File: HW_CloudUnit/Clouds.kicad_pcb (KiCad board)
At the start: 2 copper layers, 0 parts

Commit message: (WIP) Layout of driver board
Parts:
- added C1: 4.7u, Capacitor_SMD:C_0603_1608Metric, B.Cu at (22.6, 23.2)
- added C2: 100n, Capacitor_SMD:C_0603_1608Metric, B.Cu at (24.1, 23.2)
- added C3: 100n, Capacitor_SMD:C_0603_1608Metric, B.Cu at (24.6, 32.2)
- added C4: 10n, Capacitor_SMD:C_0603_1608Metric, F.Cu at (32.6, 34.1)
- added C5: 470n, Capacitor_SMD:C_0603_1608Metric, F.Cu at (36.2, 42.2)
- added C6: 100n, Capacitor_SMD:C_0603_1608Metric, F.Cu at (26.2, 36.6)
- added C7: 10u, Capacitor_SMD:CP_Elec_5x3.9, F.Cu at (27.7, 31.9)
- added D1: White, LED_SMD:LED_0603_1608Metric, F.Cu at (36.1, 34.2)
- added D2: Green, LED_SMD:LED_0603_1608Metric, F.Cu at (37.6, 34.2)
- added D3: Yellow, LED_SMD:LED_0603_1608Metric, F.Cu at (39.1, 34.2)
- added G***: LOGO, LOGO, F.Cu at (46.6, 13.7)
- added G***: LOGO, LOGO, B.Cu at (31.4, 65.4)
- added G***: LOGO, LOGO, B.Cu at (23.7, 63.8)
- added G***: LOGO, LOGO, B.Cu at (28.2, 64.1)
- added J1: Conn_01x06, Connector_PinHeader_2.54mm:PinHeader_1x06_P2.54mm_Vertical, F.Cu at (20.0, 32.7)
- added J2: Conn_01x04, Connector_JST:JST_GH_SM04B-GHS-TB_1x04-1MP_P1.25mm_Horizontal, F.Cu at (21.1, 40.2)
- added J3: Conn_01x04, Connector_PinHeader_2.00mm:PinHeader_1x04_P2.00mm_Vertical, F.Cu at (38.8, 19.8)
- added J4: Conn_01x04, Clouds_footprints:TestPoints_1x04_P2.0, F.Cu at (29.2, 19.6)
- added JP1: SolderJumper_2_Open, Jumper:SolderJumper-2_P1.3mm_Open_RoundedPad1.0x1.5mm, F.Cu at (38.4, 42.2)
- added R1: 100k, Resistor_SMD:R_0603_1608Metric, B.Cu at (34.7, 19.7)
- added R2: 2.2k, Resistor_SMD:R_0603_1608Metric, B.Cu at (35.3, 30.0)
- added R3: 2.2k, Resistor_SMD:R_0603_1608Metric, B.Cu at (33.8, 30.0)
- added R4: TBD, Resistor_SMD:R_0603_1608Metric, F.Cu at (36.1, 37.2)
- added R5: TBD, Resistor_SMD:R_0603_1608Metric, F.Cu at (37.6, 37.2)
- added R6: TBD, Resistor_SMD:R_0603_1608Metric, F.Cu at (39.1, 37.2)
- added R7: TBD, Resistor_SMD:R_0603_1608Metric, B.Cu at (35.4, 21.8)
- added R8: TBD, Resistor_SMD:R_0603_1608Metric, B.Cu at (35.4, 23.8)
- added R9: TBD, Resistor_SMD:R_0603_1608Metric, B.Cu at (35.4, 25.8)
- added U1: STM32G030F6Px, Package_SO:TSSOP-20_4.4x6.5mm_P0.65mm, B.Cu at (28.7, 24.2)
- added U2: AS5600L-ASOM, Clouds_footprints:SOIC127P600X175-8N, B.Cu at (29.2, 32.7)
- added U3: DRV8313PWPR, Clouds_footprints:SOP65P640X120-29N, F.Cu at (31.2, 39.9)
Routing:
- net NFAULT: track 0.00 -> 8.37 mm
- net MOTOR_W: track 0.00 -> 6.11 mm
- net Net-(U3-CPH): track 0.00 -> 6.05 mm
- net V3P3O: track 0.00 -> 5.66 mm
- net MOTOR_U: track 0.00 -> 5.32 mm
- net MOTOR_V: track 0.00 -> 5.06 mm
- net Net-(U3-CPL): track 0.00 -> 4.23 mm
- net Net-(U3-VCP): track 0.00 -> 2.54 mm
- net GND: track 0.00 -> 0.82 mm, vias 0 -> 22
- added copper zone on B.Cu, net GND
- added copper zone on F.Cu, net GND
- added copper zone on F.Cu, net V3P3O
- added copper zone on F.Cu, net VM
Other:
- board outline added: 22 x 27 mm
- board text added: "*"
- board text added: "+"
- board text added: "23-Flurry"
- board text added: "3V3"
- board text added: "B"
- board text added: "BLDC Driver (Y-wired) Magnet Encoder"
- board text added: "BLDC on Clouds"
- board text added: "CM"
- board text added: "CSN"
- board text added: "G"
- board text added: "GND"
- board text added: "Input 8-60 V Output 1.75 A RMS"
- board text added: "JLCJLCJLCJLC"
- board text added: "R"
- board text added: "Rev. 1"
- board text added: "SCK"
- board text added: "SDA"
- board text added: "U"
- board text added: "V"
- board text added: "VM"
- board text added: "W"

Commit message: (WIP) Try routing
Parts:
- moved R4 3.40 mm to (36.1, 33.8)
- moved R5 3.40 mm to (37.6, 33.8)
- moved R6 3.40 mm to (39.1, 33.8)
- moved D1 3.40 mm to (36.1, 30.8)
- moved D2 3.40 mm to (37.6, 30.8)
- moved D3 3.40 mm to (39.1, 30.8)
- moved C1 1.70 mm to (22.6, 24.9), turned to 90 degrees
- moved C2 1.70 mm to (24.1, 24.9), turned to 90 degrees
- moved R2 1.30 mm to (35.2, 31.3)
- moved R3 1.30 mm to (33.7, 31.3)
- turned U1 to 0 degrees
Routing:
- net +3.3V: track 0.00 -> 79.6 mm, vias 0 -> 2
- net LED_ACT: track 0.00 -> 20.9 mm, vias 0 -> 1
- net SWCLK: track 0.00 -> 14.2 mm
- net NFAULT: track 8.37 -> 20.2 mm
- net UNIT_CSN: track 0.00 -> 11.6 mm
- net LED_B: track 0.00 -> 9.51 mm, vias 0 -> 2
- net SWDIO: track 0.00 -> 7.46 mm, vias 0 -> 1
- net UNIT_SDA: track 0.00 -> 6.37 mm
- net UNIT_SCK: track 0.00 -> 6.12 mm
- net LED_G: track 0.00 -> 5.00 mm
- net V3P3O: track 5.66 -> 10.5 mm
- net MAG_SCL: track 0.00 -> 3.80 mm
- net EN_U: track 0.00 -> 3.66 mm, vias 0 -> 1
- net LED_R: track 0.00 -> 3.23 mm
- net IN_U: track 0.00 -> 3.01 mm, vias 0 -> 1
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- added copper zone on B.Cu, net +3.3V

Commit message: Finish driver board design
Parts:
- moved G*** 21.7 mm to (28.9, 43.9)
- moved G*** 21.7 mm to (21.2, 42.3)
- moved G*** 21.7 mm to (25.7, 42.6)
- moved G*** 13.9 mm to (36.8, 23.6)
- moved D1 5.00 mm to (41.1, 30.8)
- moved D2 5.00 mm to (42.6, 30.8)
- moved D3 5.00 mm to (44.1, 30.8)
- moved J3 5.00 mm to (43.8, 19.8)
- moved R4 5.00 mm to (41.1, 33.8)
- moved R5 5.00 mm to (42.6, 33.8)
- moved R6 5.00 mm to (44.1, 33.8)
- moved R7 5.00 mm to (40.4, 21.8)
- moved R8 5.00 mm to (40.4, 23.8)
- moved R9 5.00 mm to (40.4, 25.8)
- moved J4 3.50 mm to (32.7, 19.7)
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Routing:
- net EN_U: track 3.66 -> 24.7 mm
- net EN_W: track 0.00 -> 20.0 mm, vias 0 -> 1
- net EN_V: track 2.38 -> 22.3 mm
- net IN_U: track 3.01 -> 21.1 mm
- net MAG_SCL: track 3.80 -> 20.5 mm
- net IN_V: track 1.76 -> 18.5 mm
- net IN_W: track 0.00 -> 15.6 mm, vias 0 -> 1
- net MAG_SDA: track 1.82 -> 17.2 mm
- net LED_B: track 9.51 -> 17.4 mm
- net LED_ACT: track 20.9 -> 28.8 mm
- net +3.3V: track 79.6 -> 72.7 mm
- net UNIT_SCK: track 6.12 -> 9.62 mm
- net UNIT_SDA: track 6.37 -> 9.87 mm
- net UNIT_CSN: track 11.6 -> 15.1 mm
- net SWCLK: track 14.2 -> 17.2 mm
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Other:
- board size 22 x 27 mm -> 27 x 27 mm
- board text added: "BLDC (Y-wired) + Mag. Enc."
- board text added: "Close for on-board 3V3 reg."
- board text added: "In 8-50 V Out 1.75 A RMS"
- board text added: "Rev. 2"
- board text removed: "BLDC Driver (Y-wired) Magnet Encoder"
- board text removed: "Input 8-60 V Output 1.75 A RMS"
- board text removed: "Rev. 1"

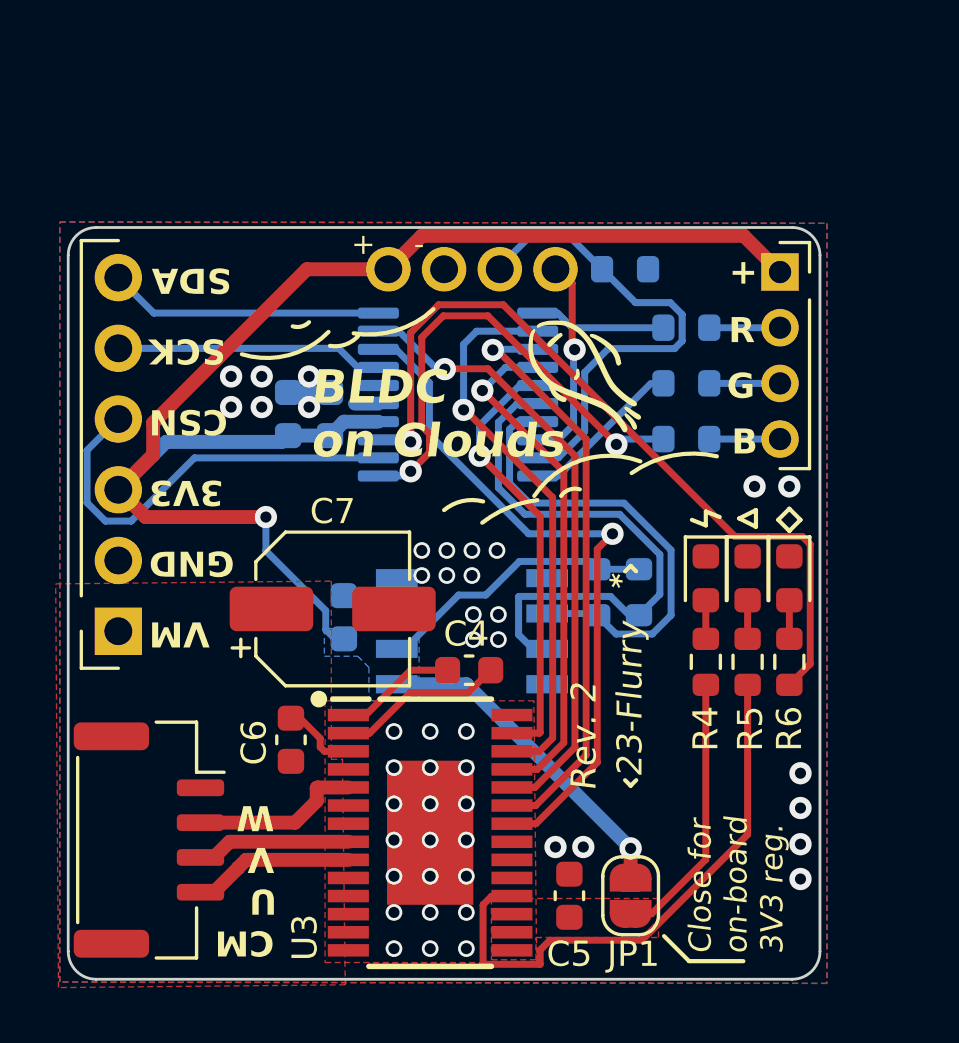
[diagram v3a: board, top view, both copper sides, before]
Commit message: Fix motor's wire order
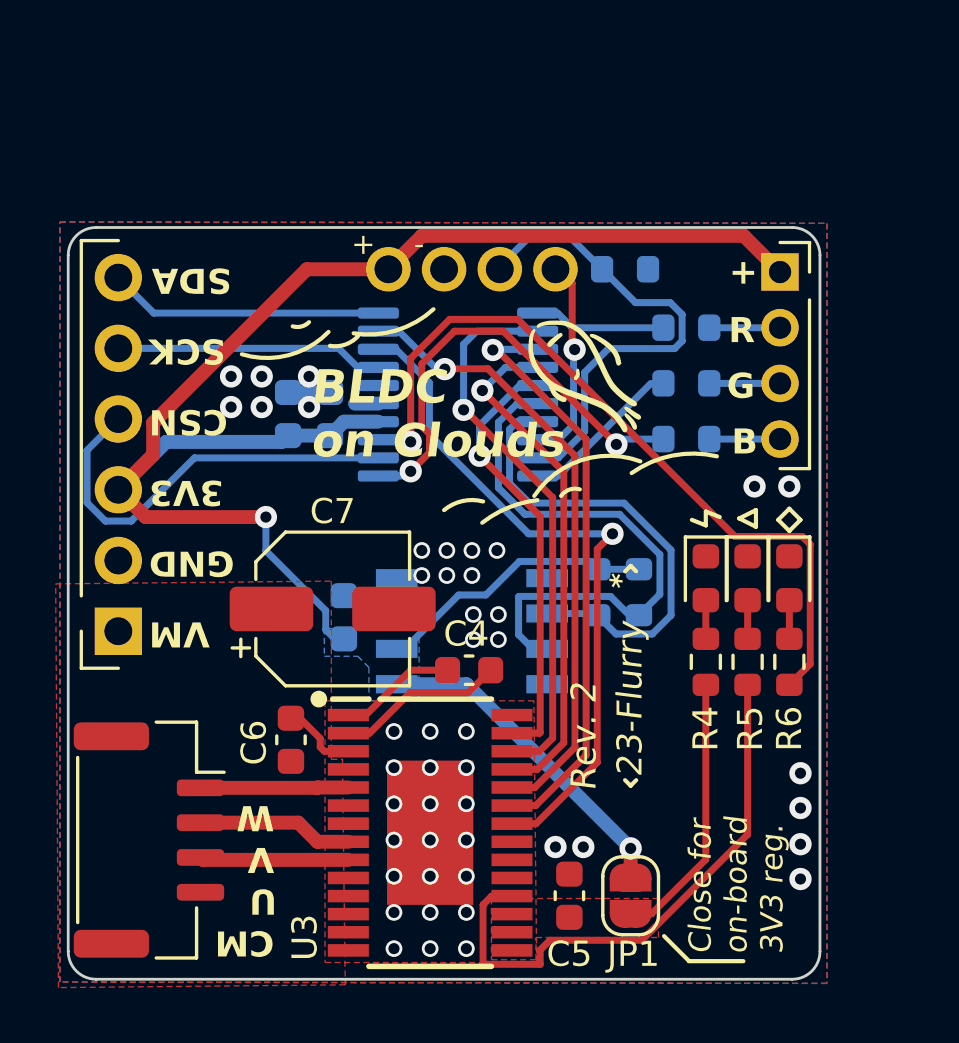
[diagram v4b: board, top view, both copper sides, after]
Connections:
- J2 pad 1: unconnected-(J2-Pin_1-Pad1) -> MOTOR_W
- J2 pad 2: MOTOR_W -> MOTOR_V
- J2 pad 3: MOTOR_V -> MOTOR_U
- J2 pad 4: MOTOR_U -> unconnected-(J2-Pin_4-Pad4)
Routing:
- net LED_B: track 17.4 -> 16.4 mm
- net LED_ACT: track 28.8 -> 27.8 mm
- net MOTOR_W: track 6.11 -> 5.32 mm
- net MOTOR_V: track 5.06 -> 5.60 mm
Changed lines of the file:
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@@
   (net 38 "Net-(J3-Pin_4)")
   (net 39 "V3P3O")
-  (net 40 "unconnected-(J2-Pin_1-Pad1)")
+  (net 40 "unconnected-(J2-Pin_4-Pad4)")
   (footprint "Connector_JST:JST_GH_SM04B-GHS-TB_1x04-1MP_P1.25mm_Horizontal" (layer "F.Cu")
     (at 21.1 40.2 -90)
@@
       (stroke (width 0.1) (type solid)) (layer "F.Fab"))
     (pad "1" smd roundrect (at -1.875 -1.85 270) (size 0.6 1.7) (layers "F.Cu" "F.Paste" "F.Mask") (roundrect_rratio 0.25)
-      (net 40 "unconnected-(J2-Pin_1-Pad1)") (pinfunction "Pin_1") (pintype "passive+no_connect"))
+      (net 15 "MOTOR_W") (pinfunction "Pin_1") (pintype "passive"))
     (pad "2" smd roundrect (at -0.625 -1.85 270) (size 0.6 1.7) (layers "F.Cu" "F.Paste" "F.Mask") (roundrect_rratio 0.25)
-      (net 15 "MOTOR_W") (pinfunction "Pin_2") (pintype "passive"))
+      (net 14 "MOTOR_V") (pinfunction "Pin_2") (pintype "passive"))
     (pad "3" smd roundrect (at 0.625 -1.85 270) (size 0.6 1.7) (layers "F.Cu" "F.Paste" "F.Mask") (roundrect_rratio 0.25)
-      (net 14 "MOTOR_V") (pinfunction "Pin_3") (pintype "passive"))
+      (net 13 "MOTOR_U") (pinfunction "Pin_3") (pintype "passive"))
     (pad "4" smd roundrect (at 1.875 -1.85 270) (size 0.6 1.7) (layers "F.Cu" "F.Paste" "F.Mask") (roundrect_rratio 0.25)
-      (net 13 "MOTOR_U") (pinfunction "Pin_4") (pintype "passive"))
+      (net 40 "unconnected-(J2-Pin_4-Pad4)") (pinfunction "Pin_4") (pintype "passive+no_connect"))
     (pad "MP" smd roundrect (at -3.725 1.35 270) (size 1 2.7) (layers "F.Cu" "F.Paste" "F.Mask") (roundrect_rratio 0.25))
     (pad "MP" smd roundrect (at 3.725 1.35 270) (size 1 2.7) (layers "F.Cu" "F.Paste" "F.Mask") (roundrect_rratio 0.25))
@@
   (segment (start 34.409314 23.875) (end 35.0625 23.875) (width 0.25) (layer "B.Cu") (net 12))
   (segment (start 32.9755 25.308814) (end 34.409314 23.875) (width 0.25) (layer "B.Cu") (net 12))
-  (segment (start 28.262 40.9125) (end 24.5875 40.9125) (width 0.5) (layer "F.Cu") (net 13))
-  (segment (start 24.5875 40.9125) (end 24.3 41.2) (width 0.5) (layer "F.Cu") (net 13))
-  (segment (start 24.3 41.2) (end 24.3 41.206974) (width 0.5) (layer "F.Cu") (net 13))
-  (segment (start 24.3 41.206974) (end 23.431974 42.075) (width 0.5) (layer "F.Cu") (net 13))
-  (segment (start 28.262 40.2625) (end 23.994474 40.2625) (width 0.5) (layer "F.Cu") (net 14))
-  (segment (start 23.994474 40.2625) (end 23.431974 40.825) (width 0.5) (layer "F.Cu") (net 14))
+  (segment (start 23.0375 40.9125) (end 28.262 40.9125) (width 0.5) (layer "F.Cu") (net 13))
+  (segment (start 22.95 40.825) (end 23.0375 40.9125) (width 0.5) (layer "F.Cu") (net 13))
+  (segment (start 26.462 39.575) (end 27.1495 40.2625) (width 0.5) (layer "F.Cu") (net 14))
+  (segment (start 27.1495 40.2625) (end 28.262 40.2625) (width 0.5) (layer "F.Cu") (net 14))
+  (segment (start 22.95 39.575) (end 26.462 39.575) (width 0.5) (layer "F.Cu") (net 14))
   (segment (start 28.262 38.3125) (end 27.1495 38.3125) (width 0.5) (layer "F.Cu") (net 15))
-  (segment (start 27.1495 38.3125) (end 27.1245 38.3375) (width 0.5) (layer "F.Cu") (net 15))
-  (segment (start 27.1245 38.3375) (end 27.1245 38.8) (width 0.5) (layer "F.Cu") (net 15))
-  (segment (start 27.1245 38.8) (end 26.3495 39.575) (width 0.5) (layer "F.Cu") (net 15))
-  (segment (start 26.3495 39.575) (end 22.95 39.575) (width 0.5) (layer "F.Cu") (net 15))
+  (segment (start 27.1495 38.3125) (end 27.137 38.325) (width 0.5) (layer "F.Cu") (net 15))
+  (segment (start 27.137 38.325) (end 22.95 38.325) (width 0.5) (layer "F.Cu") (net 15))
   (segment (start 42.6 34.625) (end 42.6 40.001468) (width 0.25) (layer "F.Cu") (net 16))
   (segment (start 35.5 43.8) (end 35.1505 44.1495) (width 0.25) (layer "F.Cu") (net 16))
@@
   (segment (start 39.124999 23.8) (end 35.799999 27.125) (width 0.25) (layer "B.Cu") (net 22))
   (segment (start 35.799999 27.125) (end 35.0625 27.125) (width 0.25) (layer "B.Cu") (net 22))
-  (segment (start 30.9 22.145405) (end 30.9 25.345405) (width 0.25) (layer "F.Cu") (net 24))
+  (segment (start 31.175 26.282819) (end 30.500978 26.956841) (width 0.25) (layer "F.Cu") (net 24))
   (segment (start 30.9 25.345405) (end 31.175 25.620405) (width 0.25) (layer "F.Cu") (net 24))
-  (segment (start 33.275 21.375) (end 31.670405 21.375) (width 0.25) (layer "F.Cu") (net 24))
-  (segment (start 37.8875 25.991388) (end 37.8875 25.9875) (width 0.25) (layer "F.Cu") (net 24))
   (segment (start 31.175 25.620405) (end 31.175 26.282819) (width 0.25) (layer "F.Cu") (net 24))
-  (segment (start 31.670405 21.375) (end 30.9 22.145405) (width 0.25) (layer "F.Cu") (net 24))
-  (segment (start 31.175 26.282819) (end 30.500978 26.956841) (width 0.25) (layer "F.Cu") (net 24))
-  (segment (start 37.8875 25.9875) (end 33.275 21.375) (width 0.25) (layer "F.Cu") (net 24))
+  (segment (start 37.8875 25.9875) (end 33.8245 21.9245) (width 0.25) (layer "F.Cu") (net 24))
+  (segment (start 32.0755 21.9245) (end 30.9 23.1) (width 0.25) (layer "F.Cu") (net 24))
+  (segment (start 37.8875 25.991388) (end 37.8875 25.9875) (width 0.25) (layer "F.Cu") (net 24))
+  (segment (start 30.9 23.1) (end 30.9 25.345405) (width 0.25) (layer "F.Cu") (net 24))
+  (segment (start 33.8245 21.9245) (end 32.0755 21.9245) (width 0.25) (layer "F.Cu") (net 24))
   (via (at 37.8875 25.991388) (size 0.8) (drill 0.4) (layers "F.Cu" "B.Cu") (net 24))
   (via (at 30.500978 26.956841) (size 0.8) (drill 0.4) (layers "F.Cu" "B.Cu") (net 24))
@@
   (segment (start 35.0625 25.175) (end 34.325001 25.175) (width 0.25) (layer "B.Cu") (net 28))
   (segment (start 34.05 27.383102) (end 34.766898 28.1) (width 0.25) (layer "B.Cu") (net 28))
-  (segment (start 30.5 21.979719) (end 31.50472 20.975) (width 0.25) (layer "F.Cu") (net 29))
-  (segment (start 30.5 25.9) (end 30.5 21.979719) (width 0.25) (layer "F.Cu") (net 29))
-  (segment (start 44.56683 29.3) (end 44.85 29.58317) (width 0.25) (layer "F.Cu") (net 29))
-  (segment (start 44.85 33.875) (end 44.1 34.625) (width 0.25) (layer "F.Cu") (net 29))
   (segment (start 44.85 29.58317) (end 44.85 33.875) (width 0.25) (layer "F.Cu") (net 29))
-  (segment (start 31.50472 20.975) (end 33.825 20.975) (width 0.25) (layer "F.Cu") (net 29))
-  (segment (start 33.825 20.975) (end 42.15 29.3) (width 0.25) (layer "F.Cu") (net 29))
   (segment (start 42.15 29.3) (end 44.56683 29.3) (width 0.25) (layer "F.Cu") (net 29))
+  (segment (start 44.56683 29.3) (end 44.85 29.58317) (width 0.25) (layer "F.Cu") (net 29))
+  (segment (start 31.9 21.5) (end 34.35 21.5) (width 0.25) (layer "F.Cu") (net 29))
+  (segment (start 30.5 22.9) (end 31.9 21.5) (width 0.25) (layer "F.Cu") (net 29))
+  (segment (start 30.5 25.9) (end 30.5 22.9) (width 0.25) (layer "F.Cu") (net 29))
+  (segment (start 44.85 33.875) (end 44.1 34.625) (width 0.25) (layer "F.Cu") (net 29))
+  (segment (start 34.35 21.5) (end 42.15 29.3) (width 0.25) (layer "F.Cu") (net 29))
   (via (at 30.5 25.9) (size 0.8) (drill 0.4) (layers "F.Cu" "B.Cu") (net 29))
   (segment (start 29.3375 25.825) (end 30.425 25.825) (width 0.25) (layer "B.Cu") (net 29))

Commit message: Update boards with NPTH screw holes
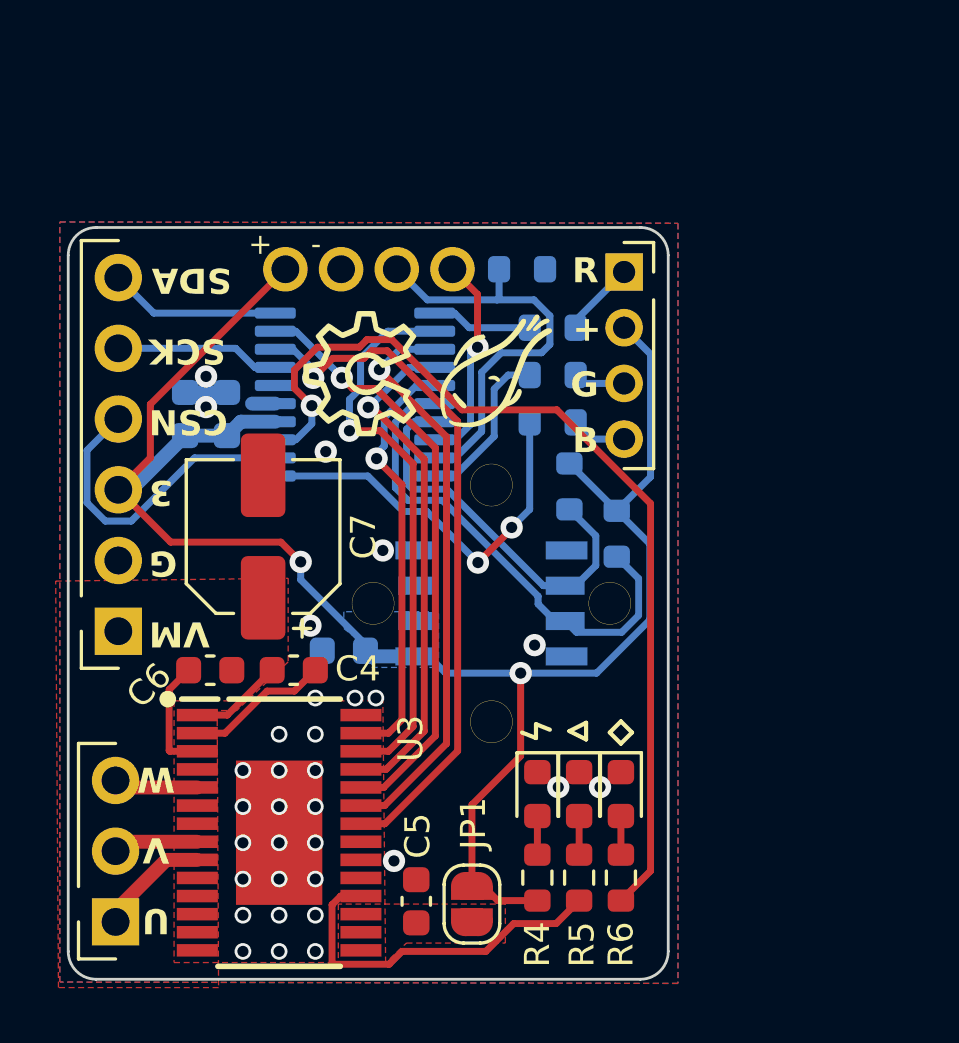
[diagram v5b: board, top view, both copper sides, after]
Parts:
- removed the G*** at (36.8, 23.6)
- removed the G*** at (28.9, 43.9)
- removed the G*** at (21.2, 42.3)
- added G***: LOGO, LOGO, F.Cu at (28.7, 23.4)
- added H1: MountingHole, Clouds_footprints:MountingHoles_M1.4_Diag8.5, F.Cu at (33.4, 31.7)
- G***: moved to F.Cu
- J2: value Conn_01x04 -> Conn_01x03; footprint Connector_JST:JST_GH_SM04B-GHS-TB_1x04-1MP_P1.25mm_Horizontal -> Connector_PinHeader_2.54mm:PinHeader_1x03_P2.54mm_Vertical
- R2, R3: value 2.2k -> 1.5k
- moved G*** 20.8 mm to (33.6, 23.3), turned to 90 degrees
- moved R4 9.83 mm to (35.0, 41.5)
- moved R5 9.83 mm to (36.5, 41.5)
- moved R6 9.83 mm to (38.0, 41.5)
- moved D1 9.83 mm to (35.0, 38.5)
- moved D2 9.83 mm to (36.5, 38.5)
- moved D3 9.83 mm to (38.0, 38.5)
- moved C4 6.30 mm to (26.3, 34.1)
- moved JP1 5.71 mm to (32.7, 42.5)
- moved J3 5.60 mm to (38.2, 19.8)
- moved C5 5.50 mm to (30.7, 42.4)
- moved U3 5.43 mm to (25.8, 39.9)
- moved R9 4.84 mm to (35.6, 25.2)
- moved R8 4.81 mm to (35.6, 23.5)
- moved R7 4.80 mm to (35.6, 21.8)
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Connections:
- J2 pad 1: MOTOR_W -> MOTOR_U
- J2 pad 3: MOTOR_U -> MOTOR_W
- J3 pad 1: +3.3V -> Net-(J3-Pin_1)
- J3 pad 2: Net-(J3-Pin_2) -> +3.3V
- R4 pad 1: V3P3O -> +3.3V
- R7 pad 1: Net-(J3-Pin_2) -> Net-(J3-Pin_1)
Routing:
- net V3P3O: track 9.78 -> 0.00 mm
- net +3.3V: track 72.7 -> 65.1 mm
- net NFAULT: track 20.4 -> 13.1 mm
- net LED_ACT: track 27.8 -> 34.1 mm
- net UNIT_SCK: track 9.62 -> 5.92 mm
- net UNIT_SDA: track 9.87 -> 6.17 mm
- net UNIT_CSN: track 15.1 -> 11.4 mm
- net MAG_SCL: track 20.5 -> 17.6 mm
- net Net-(J3-Pin_1): track 0.00 -> 2.72 mm
- net MAG_SDA: track 17.2 -> 14.6 mm
- net Net-(J3-Pin_2): track 2.54 -> 0.00 mm
- net MOTOR_V: track 5.60 -> 3.08 mm
- net MOTOR_W: track 5.32 -> 3.04 mm
- net LED_B: track 16.4 -> 14.4 mm
- net SWCLK: track 17.2 -> 15.4 mm
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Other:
- board size 27 x 27 mm -> 21.6 x 27 mm
- board text added: "3"
- board text added: "Humming Cumulus"
- board text added: "Rev. 3"
- board text removed: "3V3"
- board text removed: "BLDC (Y-wired) + Mag. Enc."
- board text removed: "BLDC on Clouds"
- board text removed: "CM"
- board text removed: "Close for on-board 3V3 reg."
- board text removed: "GND"
- board text removed: "In 8-50 V Out 1.75 A RMS"
- board text removed: "Rev. 2"
